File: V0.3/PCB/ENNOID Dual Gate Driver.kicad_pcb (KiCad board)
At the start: 2 copper layers, 60 x 98 mm, 142 parts, among them J1 Conn_02x08_Odd_Even, J10 Mounting Hole 2, J11 Mounting Hole 3, J2 Current, J3 TEMP, J4 PHASE, J5 Collector, J6 Gate_H, J7 G_L, J8 E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

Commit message: Maintenance update
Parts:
- D21: value es2j-ltp -> smcj440ca; footprint Diodes_SMD:D_SMA_Handsoldering -> Diodes_SMD:D_SMC; moved to F.Cu
- D8: value smcj440ca -> es2j-ltp; footprint Diodes_SMD:D_SMC -> Diodes_SMD:D_SMA_Handsoldering; moved to B.Cu
- moved D8 24.3 mm to (33.5, 6.35), turned to 270 degrees
- moved D5 21.0 mm to (12.8, 9.70), turned to 90 degrees
- moved D15 19.9 mm to (9.25, 6.50)
- moved D21 16.7 mm to (29.2, 6.50), turned to 0 degrees
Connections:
- D15 pad 1: PHASE -> /GD_HIGH/C
- D21 pad 1: /GD_HIGH/G -> PHASE
- D5 pad 1: /GD_LOW/G -> /GD_HIGH/G
- D8 pad 1: /GD_HIGH/C -> /GD_LOW/G
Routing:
- net Net-(D21-Pad2): track 35.8 -> 28.3 mm
- net Net-(D15-Pad2): track 28.3 -> 35.8 mm

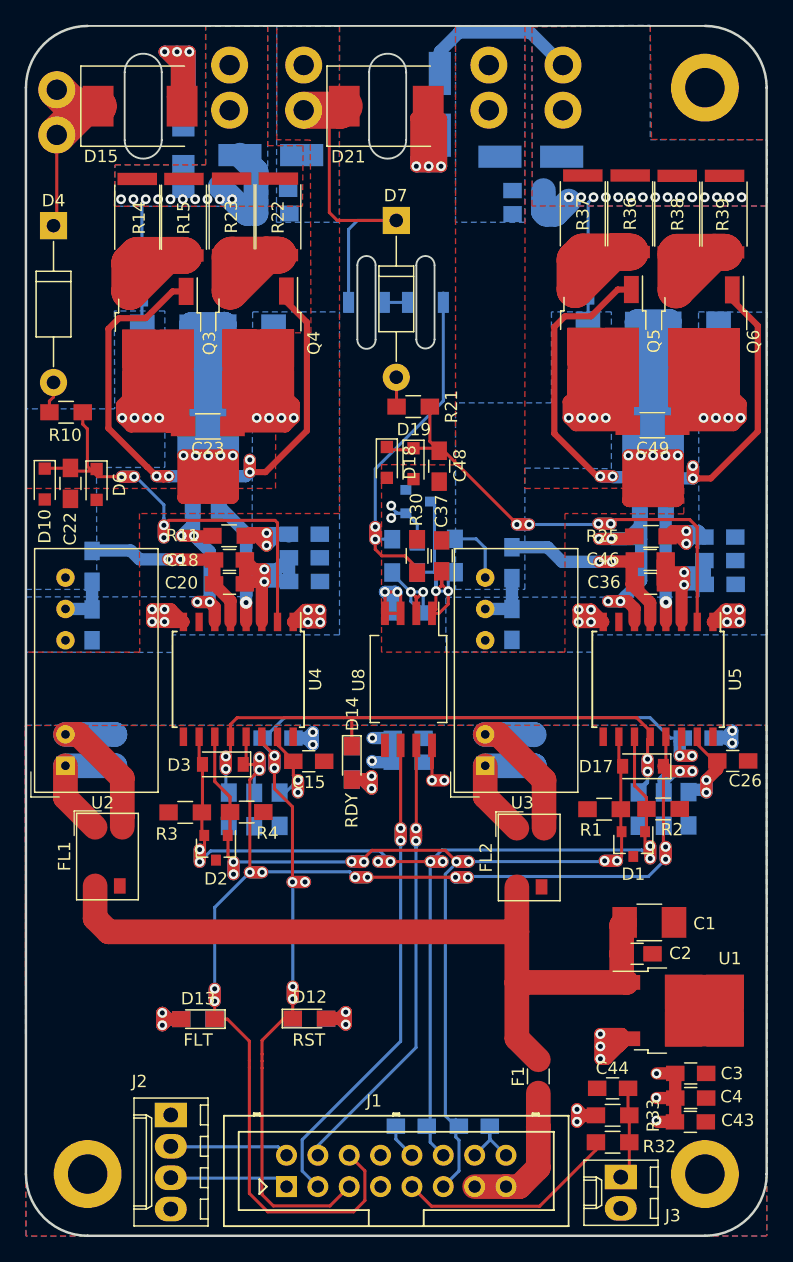
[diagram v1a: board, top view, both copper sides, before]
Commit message: V0.3 - New voltage clamping technique
Added TM4 reflex active clampiing
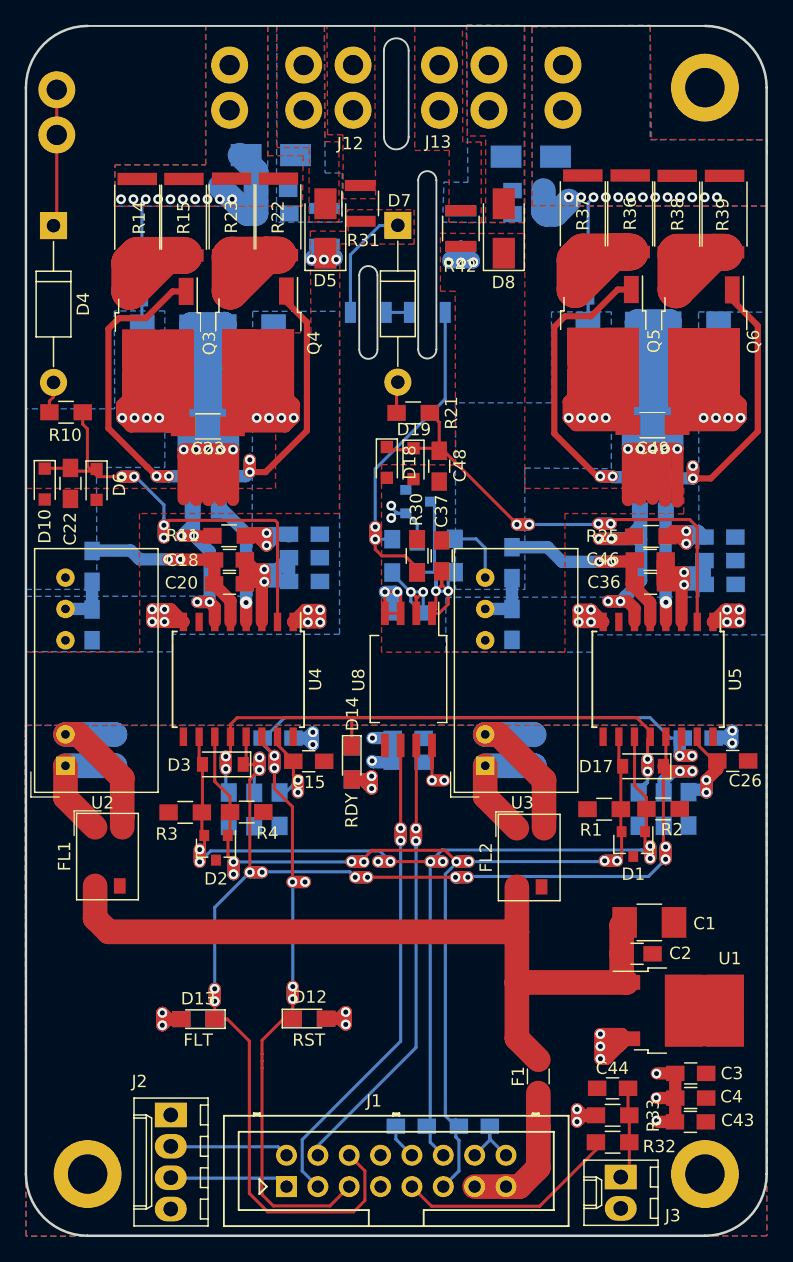
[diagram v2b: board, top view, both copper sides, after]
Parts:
- removed D15, D21: smcj440ca, Diodes_SMD:D_SMC
- added J12: E-H, ENNOID:Quick_fit_terminal, F.Cu at (26.5, 5.00)
- added J13: E-L, ENNOID:Quick_fit_terminal, F.Cu at (33.5, 5.00)
- added R19: r, Resistors_SMD:R_1210, B.Cu at (24.2, 16.2)
- added R31: r, Resistors_SMD:R_1210, F.Cu at (27.1, 14.4)
- added R41: r, Resistors_SMD:R_1210, B.Cu at (35.2, 16.4)
- added R42: r, Resistors_SMD:R_1210, F.Cu at (35.2, 16.4)
- D11, D20: footprint Diodes_SMD:D_SMA_Handsoldering -> Diodes_SMD:D_SMA
- D5, D8: value es2j-ltp -> diode; footprint Diodes_SMD:D_SMA_Handsoldering -> Diodes_SMD:D_SMA; moved to F.Cu
- moved D5 13.3 mm to (24.3, 16.4)
- moved D8 11.3 mm to (38.7, 16.4), turned to 90 degrees
- moved R27 0.83 mm to (27.7, 23.2)
- moved R29 0.83 mm to (32.5, 23.2)
- moved R21 0.51 mm to (31.4, 31.3)
- moved D7 0.42 mm to (30.1, 16.2)
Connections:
- C22 pad 2: PHASE -> /GD_LOW/C
- C24 pad 2: PHASE -> /GD_LOW/C
- C25 pad 1: PHASE -> /GD_LOW/C
- C28 pad 2: PHASE -> /GD_LOW/C
- C29 pad 1: PHASE -> /GD_LOW/C
- C30 pad 2: PHASE -> /GD_LOW/C
- C31 pad 1: PHASE -> /GD_LOW/C
- C32 pad 2: PHASE -> /GD_LOW/C
- C33 pad 1: PHASE -> /GD_LOW/C
- C58 pad 2: /ISO_PSU_LOW/COM -> /GD_LOW/E
- C7 pad 2: PHASE -> /GD_LOW/C
- C8 pad 1: PHASE -> /GD_LOW/C
- D10 pad 2: PHASE -> /GD_LOW/C
- D20 pad 2: /ISO_PSU_LOW/COM -> /GD_LOW/E
- D5 pad 1: /GD_HIGH/G -> /GD_LOW/C
- D5 pad 2: Net-(D15-Pad2) -> PHASE
- D6 pad 2: PHASE -> /GD_LOW/C
- D7 pad 1: PHASE -> /GD_LOW/C
- D8 pad 1: /GD_LOW/G -> /ISO_PSU_LOW/COM
- D8 pad 2: Net-(D21-Pad2) -> /GD_LOW/E
- J8 pad 1: /ISO_PSU_LOW/COM -> /GD_LOW/E
- R27 pad 2: PHASE -> /GD_LOW/C
- R40 pad 1: /ISO_PSU_LOW/COM -> /GD_LOW/E
- U2 pad 6: PHASE -> /GD_LOW/C
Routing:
- net PHASE: track 125.1 -> 0.65 mm, vias 5 -> 0
- net /GD_LOW/C: track 0.00 -> 110.1 mm, vias 0 -> 8
- net Net-(D15-Pad2): track 35.8 -> 0.00 mm, vias 3 -> 0
- net Net-(D21-Pad2): track 28.3 -> 0.00 mm, vias 3 -> 0
- net /ISO_PSU_LOW/COM: track 143.0 -> 120.6 mm, vias 9 -> 12
- net /GD_LOW/G: track 24.3 -> 10.9 mm, vias 15 -> 13
- net /GD_HIGH/C: track 19.9 -> 11.1 mm
- net Net-(R17-Pad1): track 30.2 -> 28.7 mm
- net Net-(C48-Pad1): track 43.8 -> 43.3 mm
- added copper zone on F.Cu, net /GD_HIGH/BUS
- added copper zone on F.Cu, net /GD_LOW/BUS
- added copper zone on F.Cu, net /GD_LOW/C
- added copper zone on B.Cu, net /GD_LOW/E
- added copper zone on F.Cu, net /GD_LOW/E
- removed copper zone on B.Cu, net /ISO_PSU_LOW/COM
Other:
- outline, holes or cut-outs redrawn
- board text added: "Dual Gate Driver - V0.3 02/2018 https://github.com/EnnoidMe"
- board text removed: "Dual Gate Driver - V0.2 01/2018 https://github.com/EnnoidMe"
